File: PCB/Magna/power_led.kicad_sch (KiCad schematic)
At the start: 10 parts

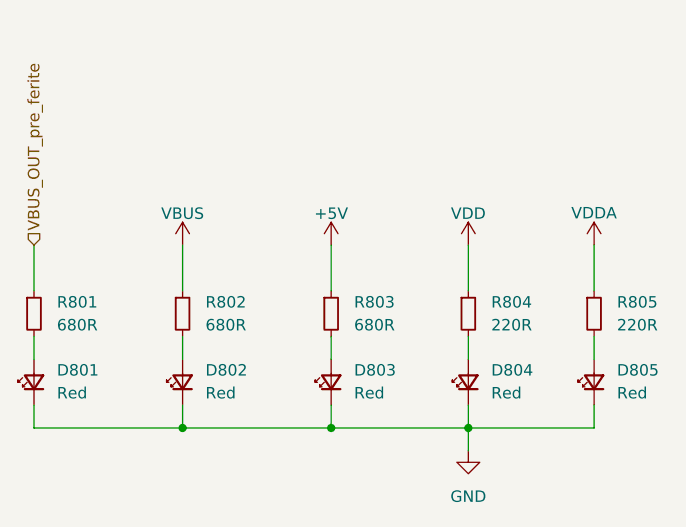
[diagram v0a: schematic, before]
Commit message: Update schematics to Kicad 9
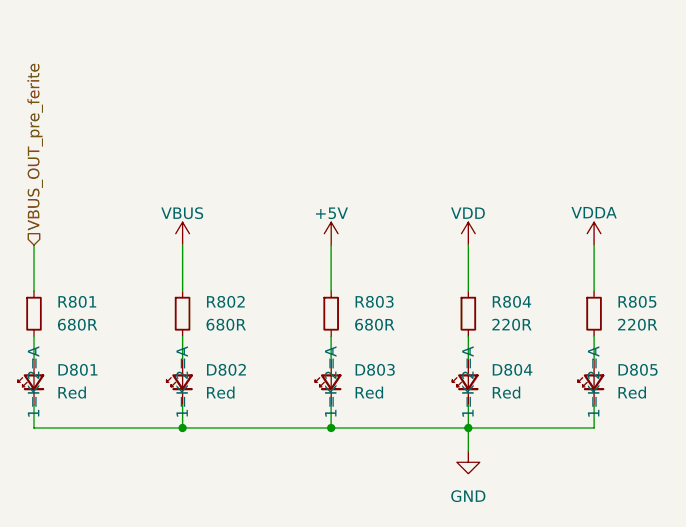
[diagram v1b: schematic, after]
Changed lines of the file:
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@@
 (kicad_sch
-	(version 20231120)
+	(version 20250114)
 	(generator "eeschema")
-	(generator_version "8.0")
+	(generator_version "9.0")
 	(paper "A4")
 	(junction
@@
 		(shape input)
 		(at 93.98 54.61 90)
-		(fields_autoplaced yes)
 		(effects
 			(font
@@
 			)
 		)
+		(property "Sim.Pin" "1=K 2=A"
+			(at 127 69.85 0)
+			(effects
+				(font
+					(size 1.27 1.27)
+				)
+			)
+		)
 		(pin "2"
 		)
@@
 			)
 		)
+		(property "Sim.Pin" "1=K 2=A"
+			(at 93.98 69.85 0)
+			(effects
+				(font
+					(size 1.27 1.27)
+				)
+			)
+		)
 		(pin "2"
 		)
@@
 			)
 		)
+		(property "Sim.Pin" "1=K 2=A"
+			(at 110.49 69.85 0)
+			(effects
+				(font
+					(size 1.27 1.27)
+				)
+			)
+		)
 		(pin "2"
 		)
@@
 			)
 		)
+		(property "Sim.Pin" "1=K 2=A"
+			(at 142.24 69.85 0)
+			(effects
+				(font
+					(size 1.27 1.27)
+				)
+			)
+		)
 		(pin "2"
 		)
@@
 			)
 		)
+		(property "Sim.Pin" "1=K 2=A"
+			(at 156.21 69.85 0)
+			(effects
+				(font
+					(size 1.27 1.27)
+				)
+			)
+		)
